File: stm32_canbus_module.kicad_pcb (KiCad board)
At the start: 2 copper layers, 33 x 33 mm, 21 parts, among them J11 Conn_01x10, J5 Conn_01x10, J6 Conn_01x10, J7 Conn_01x10, U1 STM32L431CCTx, U2 TLE9251, U3 AP7384-33Y, X1 ASE-8.000MHZ-LC-T

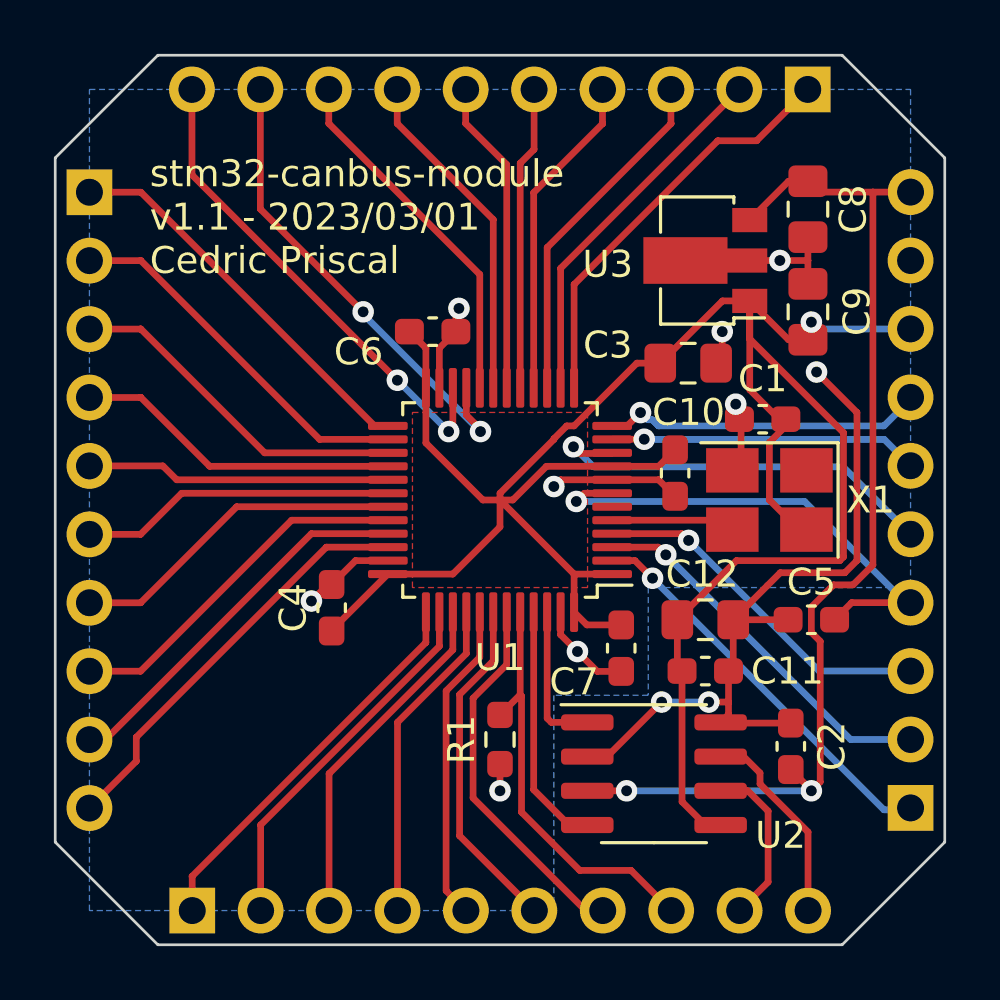
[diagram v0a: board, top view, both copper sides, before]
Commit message: 2.0
- Adding 5V regulator, VIN now supports 12V
- Migration to KiCad 9
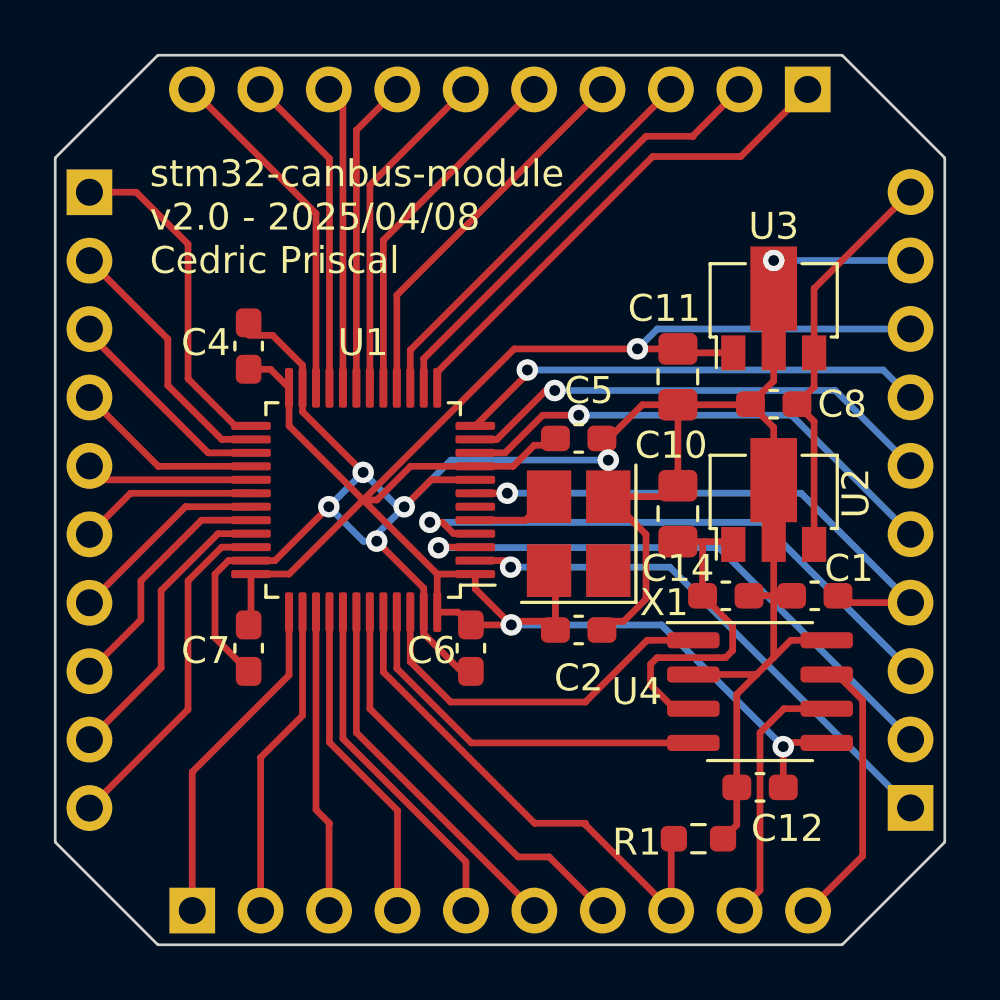
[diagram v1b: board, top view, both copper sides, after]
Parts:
- removed the C12 at (152.1, 101.8)
- removed C3: 4.7uF, Capacitor_SMD:C_0805_2012Metric_Pad1.18x1.45mm_HandSolder
- added C10: 10uF, Capacitor_SMD:C_0805_2012Metric_Pad1.18x1.45mm_HandSolder, F.Cu at (151.1, 97.8)
- added U2: AP7384-33Y, Package_TO_SOT_SMD:SOT-89-3, F.Cu at (154.6, 97.3)
- C11: renamed from C9; value 1uF -> 10uF
- C8: value 1uF -> 2.2uF; footprint Capacitor_SMD:C_0805_2012Metric_Pad1.18x1.45mm_HandSolder -> Capacitor_SMD:C_0603_1608Metric_Pad1.08x0.95mm_HandSolder
- moved C7 17.1 mm to (135.1, 102.8)
- moved C5 11.1 mm to (147.4, 95.0), turned to 0 degrees
- moved C2 10.4 mm to (147.4, 102.1), turned to 0 degrees
- moved R1 8.24 mm to (151.8, 109.9), turned to 180 degrees
- moved C8 7.35 mm to (154.6, 93.7), turned to 180 degrees
- moved X1 7.19 mm to (147.4, 98.6), turned to 90 degrees
- moved C4 6.85 mm to (135.1, 91.6), turned to 90 degrees
- moved C14 6.09 mm to (152.9, 100.9), turned to 0 degrees
- moved C6 5.58 mm to (143.4, 102.8)
- moved C11 5.40 mm to (151.1, 92.7), turned to -90 degrees
- moved U1 5.08 mm to (139.4, 97.3)
- moved U4 4.98 mm to (154.1, 104.4)
- moved C12 4.77 mm to (154.1, 108.0), turned to 180 degrees
- moved U3 3.10 mm to (154.6, 90.2), turned to 90 degrees
- moved C1 0.90 mm to (156.2, 100.9)
- renumbered C5 to C1, C11 to C12, C2 to C14, C1 to C2, C6 to C4, C4 to C5, C7 to C6, C10 to C7, J6 to J1, J7 to J2, J5 to J3, J11 to J4, U2 to U4
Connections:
- C8 pad 1: 5V -> VIN
- J4 pad 10: 5V -> VIN
- U3 pad 3: 5V -> VIN
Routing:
- net GND: track 52.1 -> 92.6 mm, vias 11 -> 6
- net 5V: track 40.0 -> 11.8 mm, vias 2 -> 0
- net VIN: track 0.00 -> 15.1 mm
- net 3V3: track 89.4 -> 79.1 mm, vias 1 -> 3
- net PC15: track 13.2 -> 22.0 mm
- net CAN_TX: track 5.49 -> 13.9 mm
- net PC14: track 14.0 -> 21.8 mm
- net PA1: track 11.5 -> 18.1 mm
- net PB10: track 18.1 -> 12.1 mm, vias 2 -> 0
- net PB11: track 18.3 -> 13.0 mm, vias 2 -> 0
- net CAN_RX: track 9.13 -> 14.2 mm
- net PB15: track 12.1 -> 7.06 mm
- net PA8: track 11.3 -> 6.21 mm
- net PA9: track 11.7 -> 6.63 mm
- net PA10: track 12.6 -> 7.47 mm
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- removed copper zone on F.Cu, net 3V3
- removed copper zone on B.Cu, net GND
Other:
- board text added: "12V"
- board text added: "3V3"
- board text added: "BOOT0"
- board text added: "CANH"
- board text added: "CANL"
- board text added: "GND"
- board text added: "PA0"
- board text added: "PA1"
- board text added: "PA10"
- board text added: "PA11"
- board text added: "PA12"
- board text added: "PA15"
- board text added: "PA2"
- board text added: "PA3"
- board text added: "PA4"
- board text added: "PA5"
- board text added: "PA6"
- board text added: "PA7"
- board text added: "PA8"
- board text added: "PA9"
- board text added: "PB0"
- board text added: "PB1"
- board text added: "PB10"
- board text added: "PB11"
- board text added: "PB12"
- board text added: "PB13"
- board text added: "PB14"
- board text added: "PB15"
- board text added: "PB2"
- board text added: "PB3"
- board text added: "PB4"
- board text added: "PB5"
- board text added: "PB6"
- board text added: "PB7"
- board text added: "PC13"
- board text added: "PC14"
- board text added: "PC15"
- board text added: "SWCLK"
- board text added: "SWDIO"
- board text added: "stm32-canbus-module v2.0 - 2025/04/08 Cedric Priscal"
- board text added: "~{RST}"
- board text removed: "stm32-canbus-module v1.1 - 2023/03/01 Cedric Priscal"
